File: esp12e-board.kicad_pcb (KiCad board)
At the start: 2 copper layers, 21.3 x 33 mm, 7 parts, among them J1 Header, U1 AMS1117-3.3, U2 ESP-12E

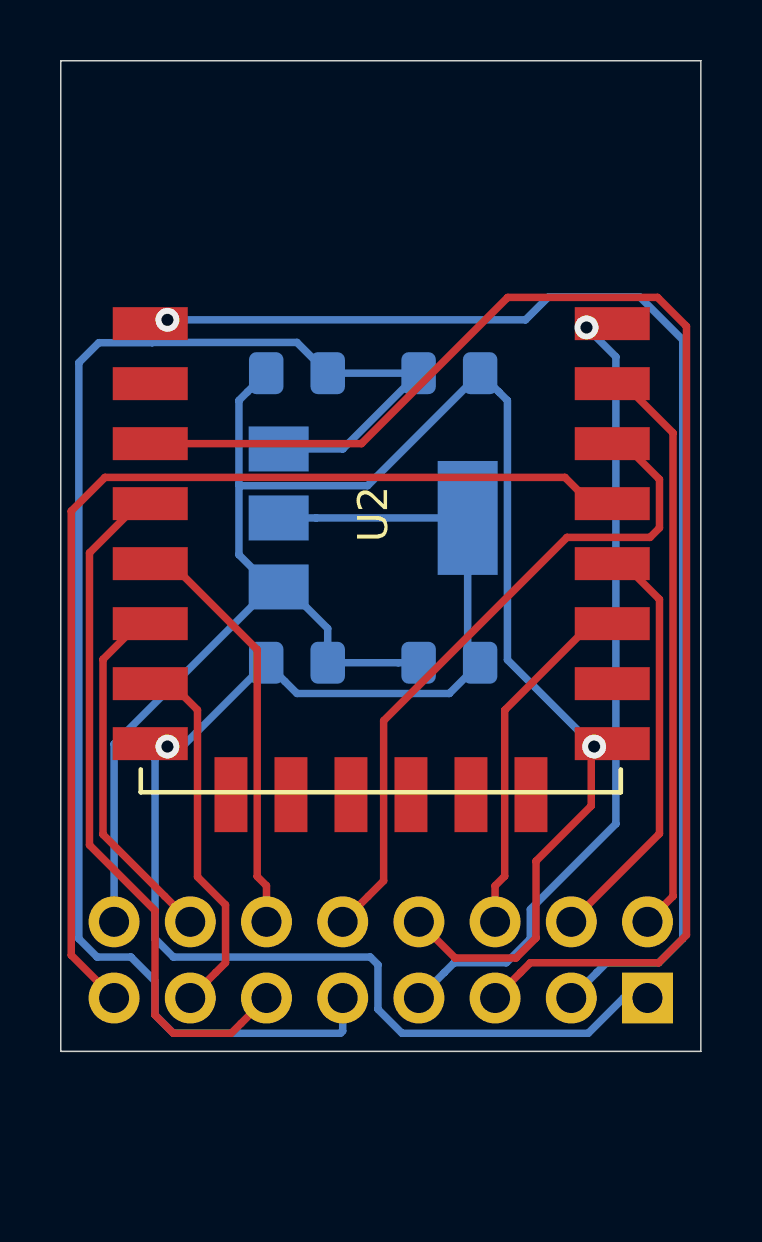
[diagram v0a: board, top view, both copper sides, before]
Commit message: adds necessary pull up/down resistors to pins to be able to boot
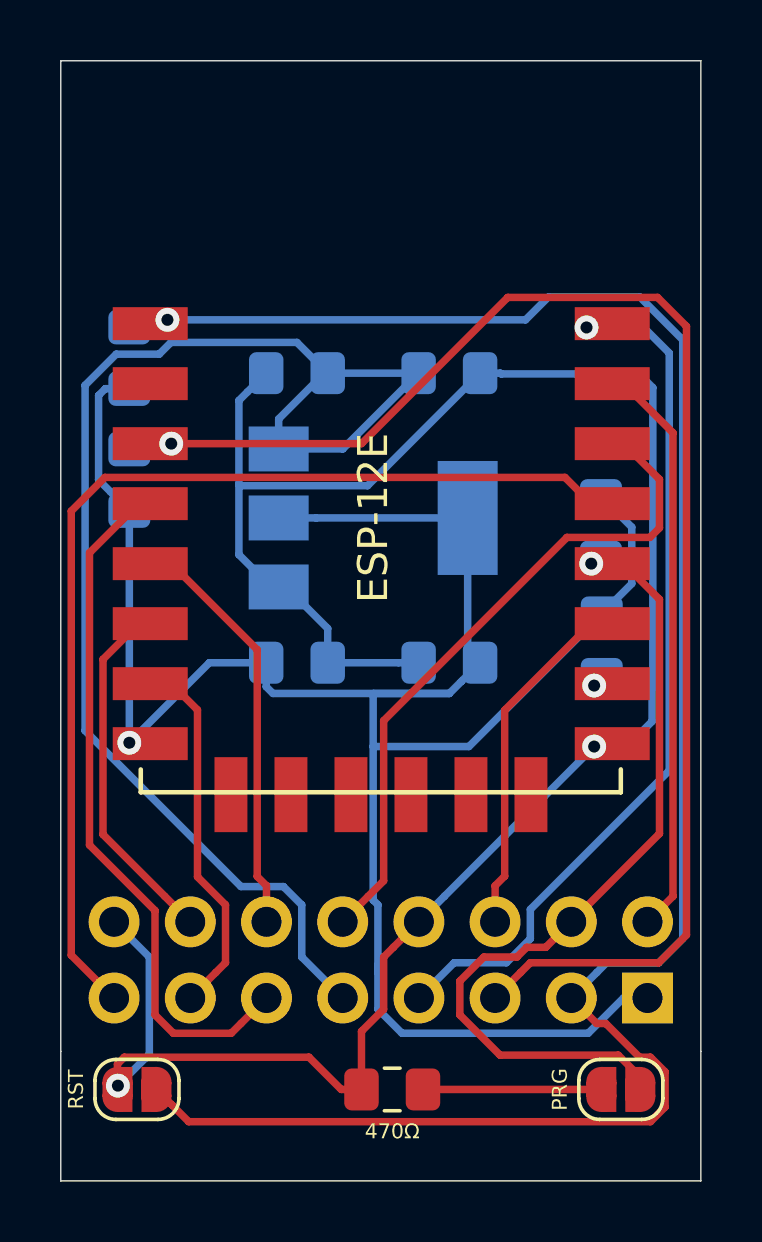
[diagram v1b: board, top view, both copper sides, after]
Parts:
- added R1: 10kΩ, Resistor_SMD:R_0805_2012Metric_Pad1.15x1.40mm_HandSolder, B.Cu at (134.4, 86.6)
- added R2: 10kΩ, Resistor_SMD:R_0805_2012Metric_Pad1.15x1.40mm_HandSolder, B.Cu at (134.4, 82.5)
- added R3: 10kΩ, Resistor_SMD:R_0805_2012Metric_Pad1.15x1.40mm_HandSolder, B.Cu at (150.1, 88.2)
- added R4: 10kΩ, Resistor_SMD:R_0805_2012Metric_Pad1.15x1.40mm_HandSolder, B.Cu at (150.1, 92.1)
- added R5: 470Ω, Resistor_SMD:R_0805_2012Metric_Pad1.15x1.40mm_HandSolder, F.Cu at (143.1, 106.9)
- added SW1: RST, Jumper:SolderJumper-2_P1.3mm_Open_RoundedPad1.0x1.5mm, F.Cu at (134.6, 106.9)
- added SW2: PRG, Jumper:SolderJumper-2_P1.3mm_Open_RoundedPad1.0x1.5mm, F.Cu at (150.7, 106.9)
- U1: value AMS1117-3.3 -> AMS1117
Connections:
- U2 pad 10: (no net) -> Net-(R4-Pad2)
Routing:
- net +3.3V: track 49.4 -> 75.9 mm
- net Net-(J1-Pad3): track 42.6 -> 66.9 mm
- net Net-(J1-Pad4): track 14.7 -> 28.1 mm, vias 0 -> 1
- net GND: track 63.5 -> 74.6 mm, vias 1 -> 2
- net Net-(R5-Pad1): track 0.00 -> 5.94 mm
- net +5V: track 48.9 -> 46.0 mm
- net Net-(J1-Pad7): track 26.5 -> 29.1 mm
- net Net-(J1-Pad5): track 47.1 -> 48.6 mm, vias 0 -> 1
- net Net-(R4-Pad2): track 0.00 -> 0.45 mm, vias 0 -> 1
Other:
- board size 21.3 x 33 mm -> 21.3 x 37.3 mm

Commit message: rewiring and changed pads to switches
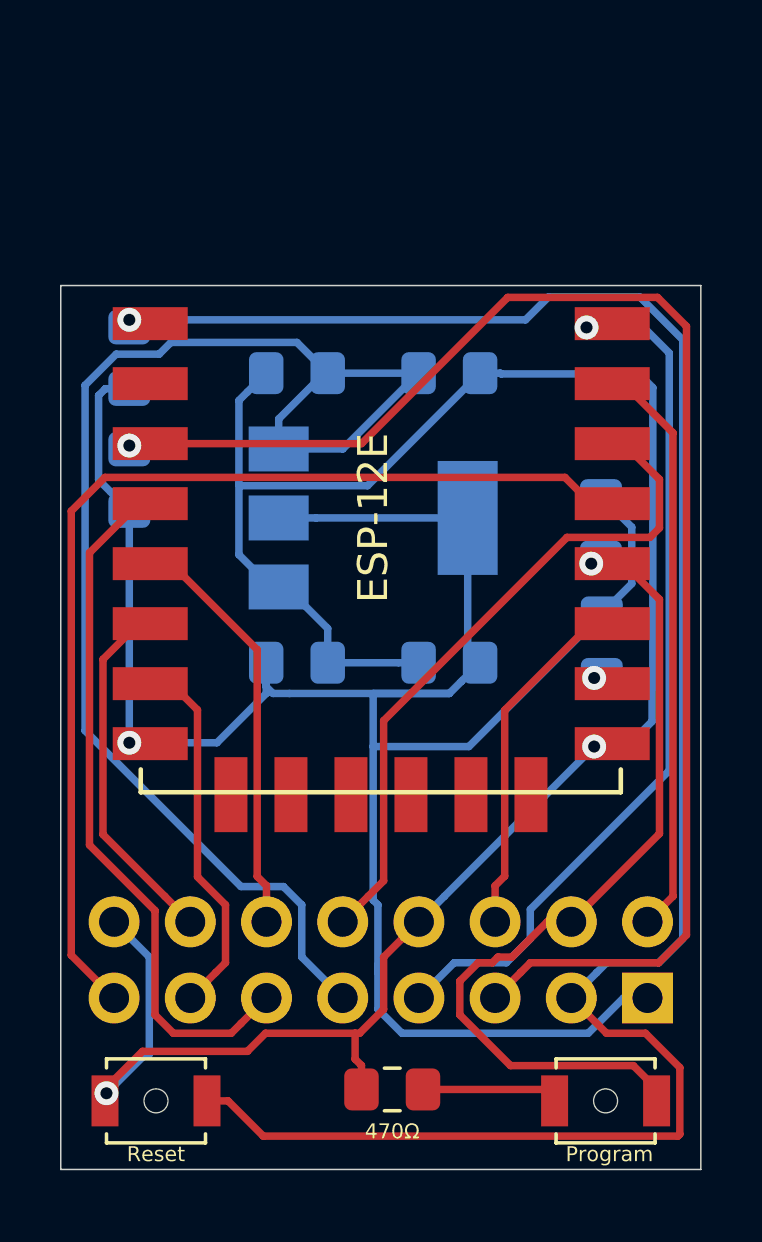
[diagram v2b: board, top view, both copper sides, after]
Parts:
- SW1: value RST -> Reset; footprint Jumper:SolderJumper-2_P1.3mm_Open_RoundedPad1.0x1.5mm -> Button_Switch_SMD:SW_SPST_B3U-1000P-B
- SW2: value PRG -> Program; footprint Jumper:SolderJumper-2_P1.3mm_Open_RoundedPad1.0x1.5mm -> Button_Switch_SMD:SW_SPST_B3U-1000P-B
- U1: value AMS1117 -> AMS1117-3.3
- moved SW1 0.74 mm to (135.3, 107.3)
- moved SW2 0.63 mm to (150.2, 107.3)
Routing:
- net Net-(J1-Pad5): track 48.6 -> 47.1 mm
- net Net-(R5-Pad1): track 5.94 -> 4.54 mm
- net GND: track 74.6 -> 75.4 mm
- net Net-(J1-Pad4): track 28.1 -> 28.8 mm
- net +3.3V: track 75.9 -> 76.5 mm
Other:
- board size 21.3 x 37.3 mm -> 21.3 x 29.5 mm

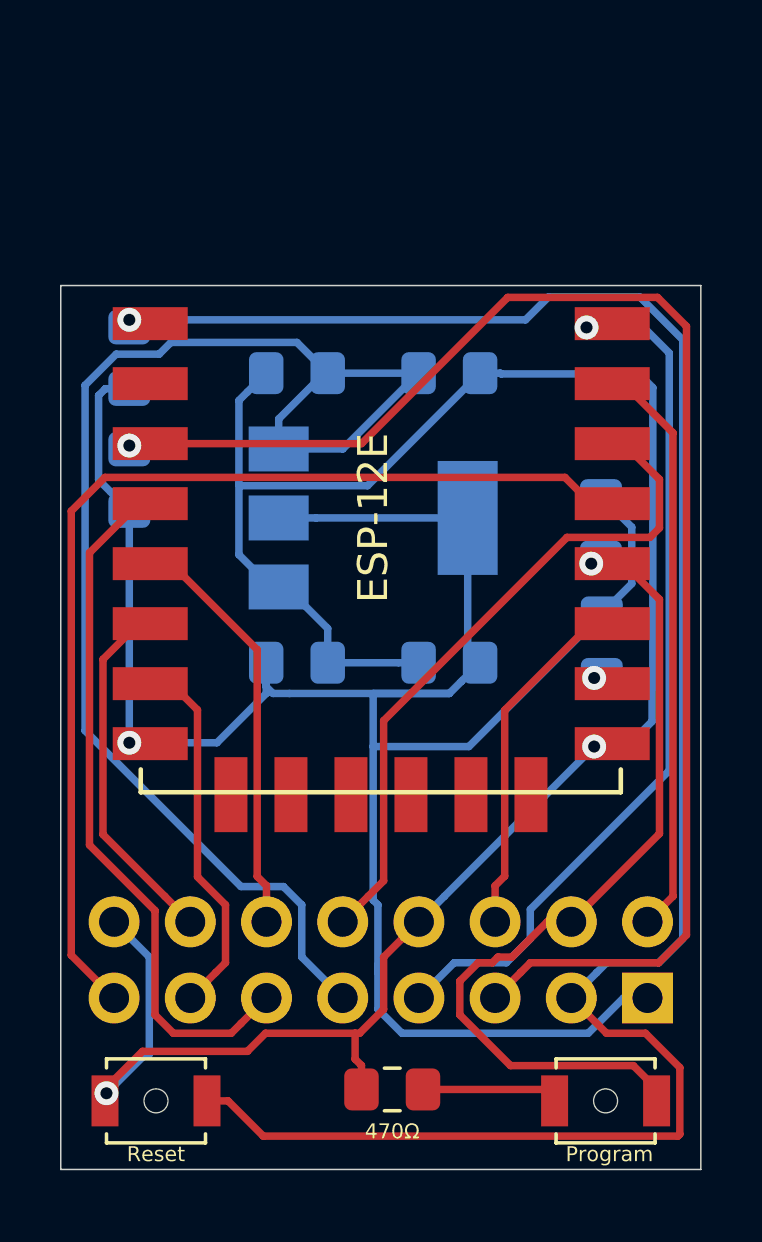
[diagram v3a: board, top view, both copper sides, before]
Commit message: fixes booting - io15 should be pulled down
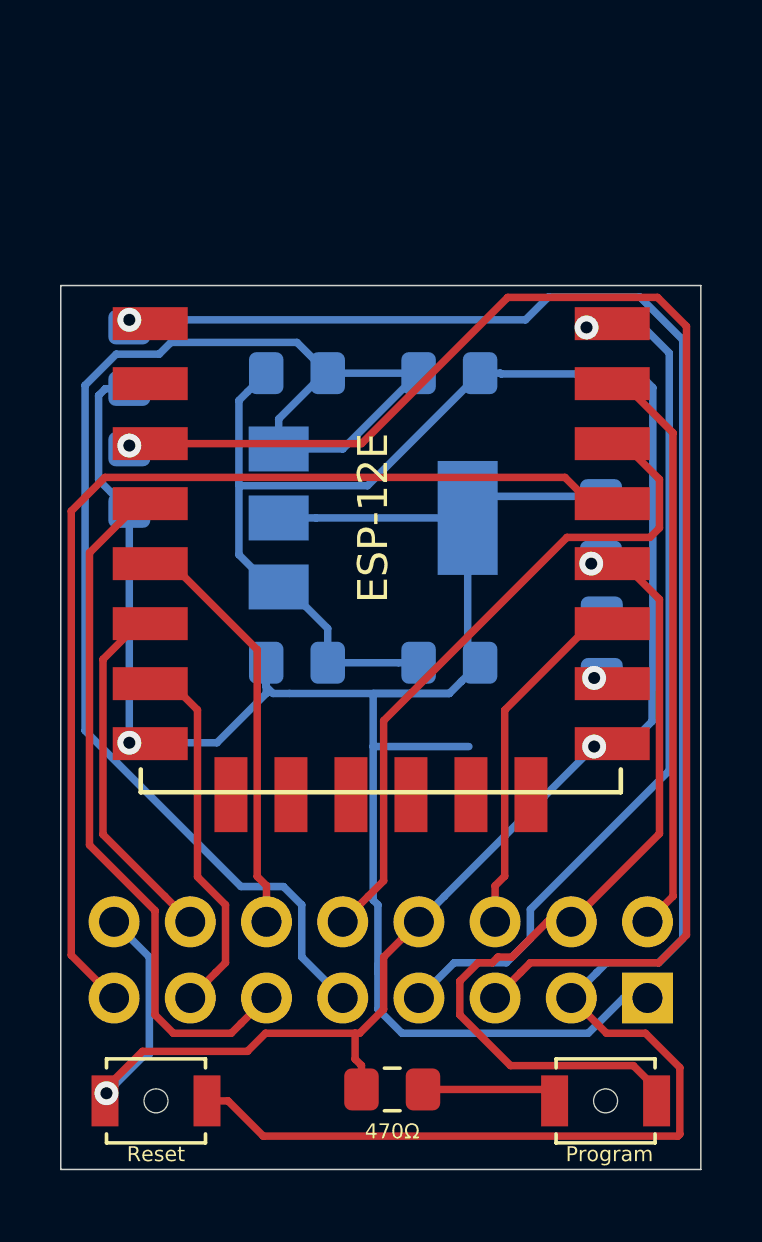
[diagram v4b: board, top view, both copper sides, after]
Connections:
- R4 pad 1: +3.3V -> GND
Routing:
- net +3.3V: track 76.5 -> 70.2 mm
- net GND: track 75.4 -> 77.1 mm
